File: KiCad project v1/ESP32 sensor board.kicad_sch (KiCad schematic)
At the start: 29 parts, among them J1 USB_C_Receptacle, J3 JST_2mm_LiPo, U1 MCP73871, U2 AMS1117-3.3

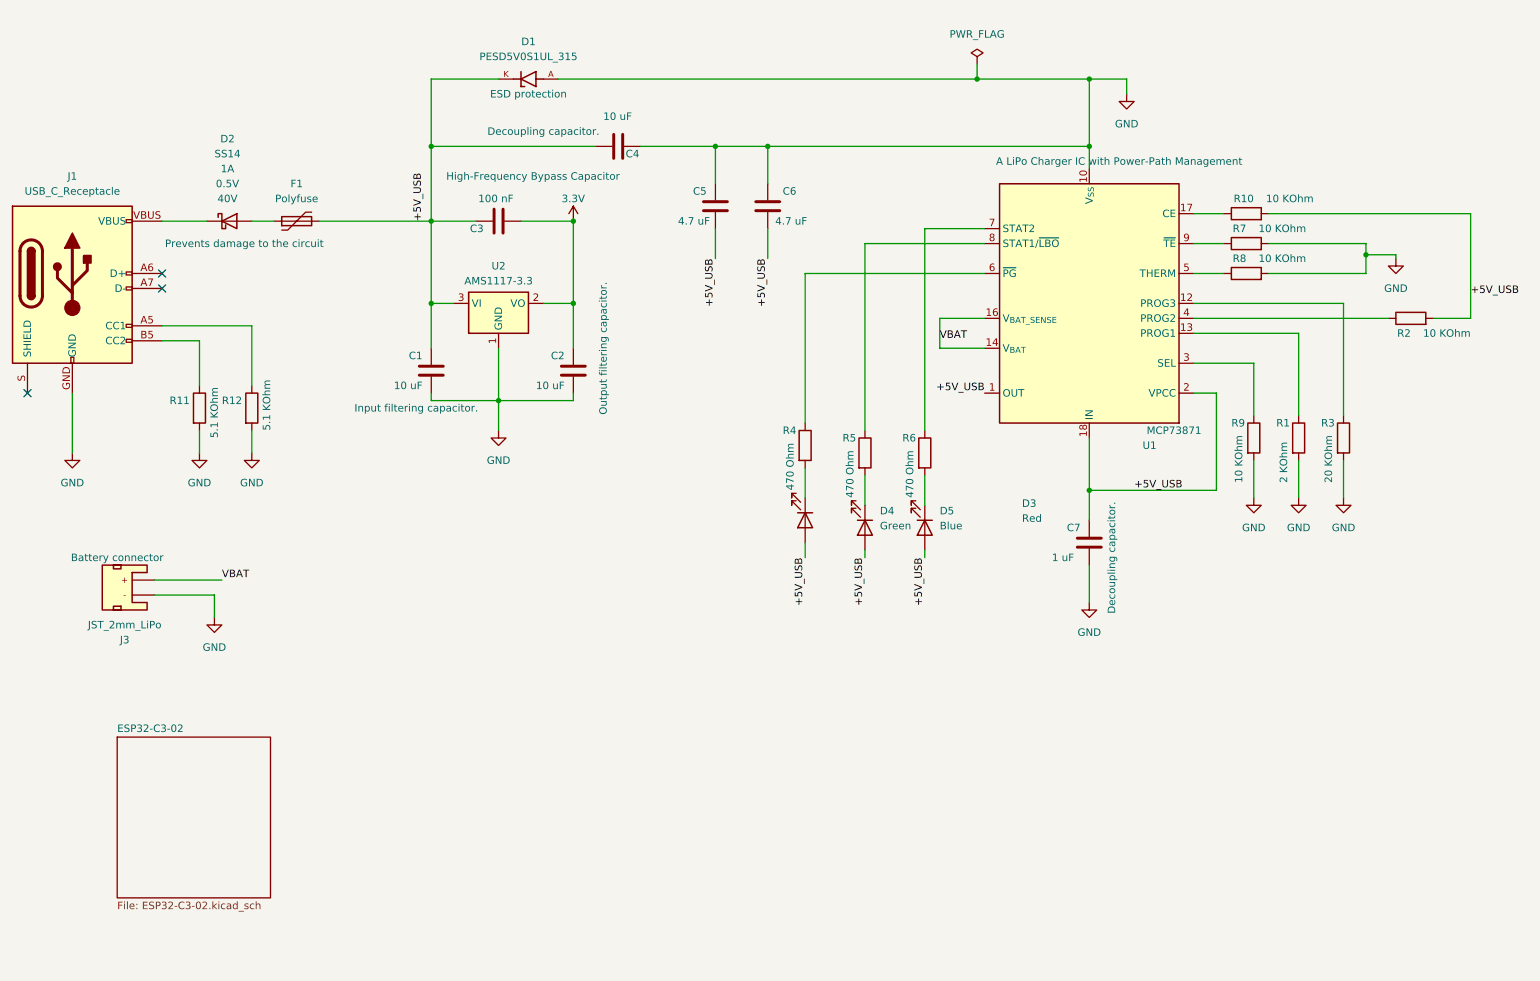
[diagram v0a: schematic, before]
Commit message: Completed first revision of the ESP32 and CP2102 integration.
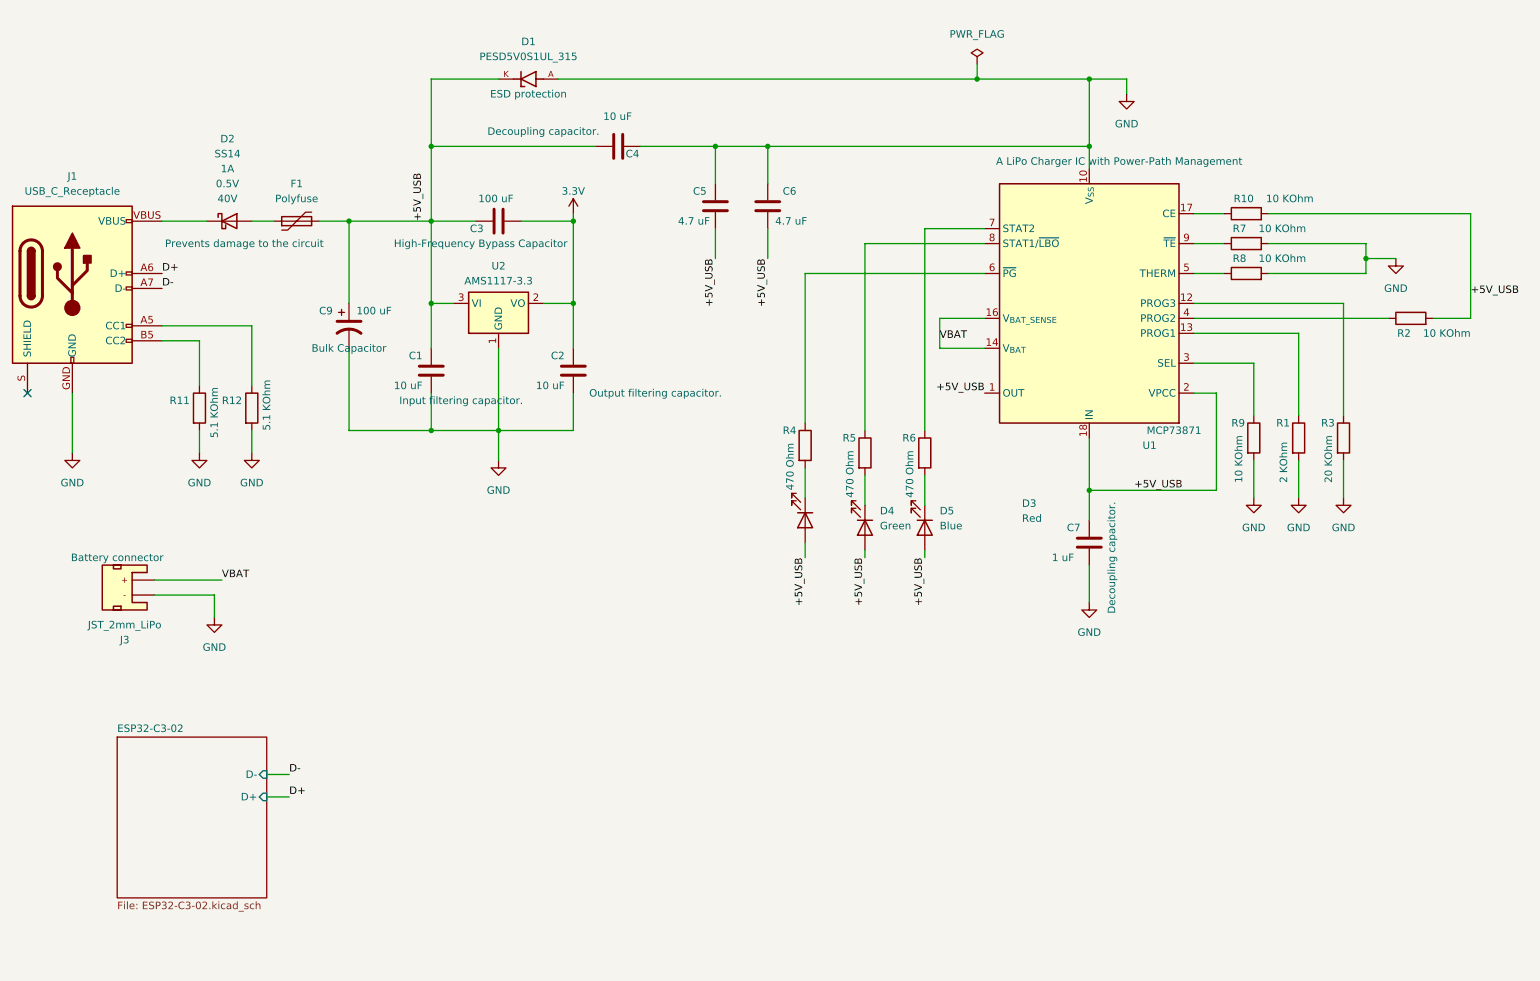
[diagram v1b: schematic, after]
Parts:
- added C9: 100 uF, Capacitor_SMD:C_0805_2012Metric, symbol SparkFun-Capacitor:C_Polarized
- C3: value 100 nF -> 100 uF
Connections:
- net +5V_USB: now also C9.1
- net GND: now also C9.2
- net D+: now reaches J1.A6 (D+), J1.B6 (D+)
- net D-: now reaches J1.A7 (D-), J1.B7 (D-)
- no-connect marks 3 -> 1
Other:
- sheet ESP32-C3-02 ports: added D+, D-; removed none

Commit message: Created the draft layout, and inserted available footprints.
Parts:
- D1: footprint PESD5V0S1UL_315:DIO_PESD5V0S1UL_315 -> Footprints:DIO_PESD5V0S1UL_315
- F1: footprint (none) -> SparkFun-Fuse:1210; symbol Device:Polyfuse -> SparkFun-Fuse:Fuse 6V/2.0A/4.0A; PROD_ID (none) -> RES-14313
- R1, R10, R11, R12, R2, R3, R4, R5, R6, R7, R8, R9: footprint (none) -> Resistor_SMD:R_0805_2012Metric
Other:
- moved on the sheet: F1
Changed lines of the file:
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@@
 			)
 		)
-		(property "Footprint" ""
+		(property "Footprint" "Resistor_SMD:R_0805_2012Metric"
 			(at 236.982 99.06 90)
 			(effects
@@
 			)
 		)
-		(property "Footprint" ""
+		(property "Footprint" "Resistor_SMD:R_0805_2012Metric"
 			(at 229.362 99.06 90)
 			(effects
@@
 			)
 		)
-		(property "Footprint" ""
+		(property "Footprint" "Resistor_SMD:R_0805_2012Metric"
 			(at 229.87 72.898 90)
 			(effects
@@
 			)
 		)
-		(property "Footprint" ""
+		(property "Footprint" "Resistor_SMD:R_0805_2012Metric"
 			(at 153.162 100.33 90)
 			(effects
@@
 			)
 		)
-		(property "Footprint" "PESD5V0S1UL_315:DIO_PESD5V0S1UL_315"
+		(property "Footprint" "Footprints:DIO_PESD5V0S1UL_315"
 			(at 107.95 38.1 0)
 			(effects
@@
 			)
 		)
-		(property "Footprint" ""
+		(property "Footprint" "Resistor_SMD:R_0805_2012Metric"
 			(at 257.81 80.518 90)
 			(effects
@@
 			)
 		)
-		(property "Footprint" ""
+		(property "Footprint" "Resistor_SMD:R_0805_2012Metric"
 			(at 50.292 93.98 90)
 			(effects
@@
 			)
 		)
-		(property "Footprint" ""
+		(property "Footprint" "Resistor_SMD:R_0805_2012Metric"
 			(at 229.87 62.738 90)
 			(effects
@@
 			)
 		)
-		(property "Footprint" ""
+		(property "Footprint" "Resistor_SMD:R_0805_2012Metric"
 			(at 163.322 101.6 90)
 			(effects
@@
 			)
 		)
-		(property "Footprint" ""
+		(property "Footprint" "Resistor_SMD:R_0805_2012Metric"
 			(at 244.602 99.06 90)
 			(effects
@@
 			)
 		)
-		(property "Footprint" ""
+		(property "Footprint" "Resistor_SMD:R_0805_2012Metric"
 			(at 59.182 93.98 90)
 			(effects
@@
 			)
 		)
-		(property "Footprint" ""
+		(property "Footprint" "Resistor_SMD:R_0805_2012Metric"
 			(at 229.87 67.818 90)
 			(effects
@@
 	)
 	(symbol
-		(lib_id "Device:Polyfuse")
-		(at 68.58 62.23 90)
+		(lib_id "SparkFun-Fuse:Fuse 6V/2.0A/4.0A")
+		(at 68.58 62.23 180)
 		(unit 1)
 		(exclude_from_sim no)
@@
 		(fields_autoplaced yes)
 		(property "Reference" "F1"
-			(at 68.58 55.88 90)
+			(at 68.58 55.88 0)
 			(effects
 				(font
@@
 		)
 		(property "Value" "Polyfuse"
-			(at 68.58 58.42 90)
+			(at 68.58 58.42 0)
 			(effects
 				(font
@@
 			)
 		)
-		(property "Footprint" ""
-			(at 73.66 60.96 0)
+		(property "Footprint" "SparkFun-Fuse:1210"
+			(at 68.58 54.61 0)
 			(effects
 				(font
 					(size 1.27 1.27)
 				)
-				(justify left)
 				(hide yes)
 			)
 		)
-		(property "Datasheet" "~"
+		(property "Datasheet" "https://www.belfuse.com/resources/datasheets/circuitprotection/ds-cp-0zch-series.pdf"
+			(at 67.564 56.642 0)
+			(effects
+				(font
+					(size 1.27 1.27)
+				)
+				(hide yes)
+			)
+		)
+		(property "Description" "Resettable fuse 2A"
 			(at 68.58 62.23 0)
 			(effects
@@
 			)
 		)
-		(property "Description" "Resettable fuse, polymeric positive temperature coefficient"
+		(property "Purpose" ""
+			(at 68.58 62.23 0)
+			(effects
+				(font
+					(size 1.27 1.27)
+				)
+			)
+		)
+		(property "Instructions and notes" ""
 			(at 68.58 62.23 0)
 			(effects
@@
 			)
 		)
+		(property "PROD_ID" "RES-14313"
+			(at 68.58 52.07 0)
+			(effects
+				(font
+					(size 1.27 1.27)
+				)
+				(hide yes)
+			)
+		)
 		(pin "1"
 		)
@@
 			)
 		)
-		(property "Footprint" ""
+		(property "Footprint" "Resistor_SMD:R_0805_2012Metric"
 			(at 173.482 101.6 90)
 			(effects

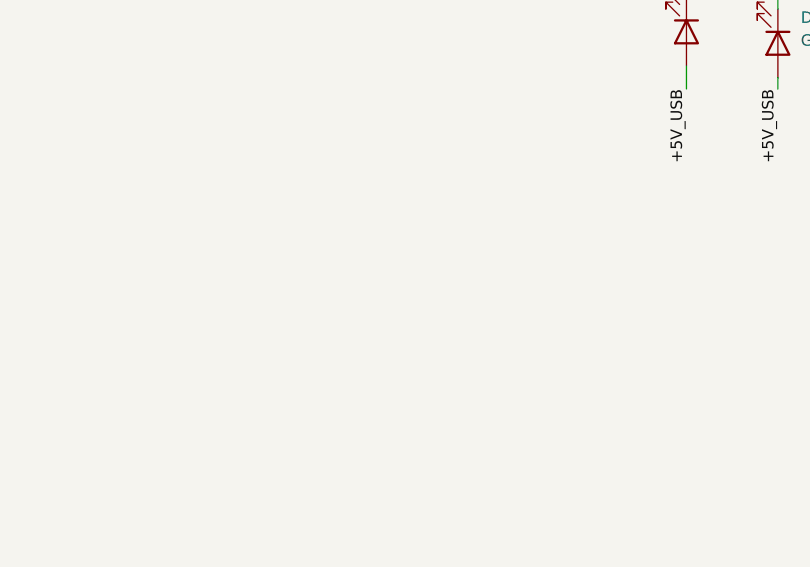
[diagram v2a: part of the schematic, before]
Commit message: Added flash memory module and microsd module to the designed. Moved the libraries and datasheets in the project folder.
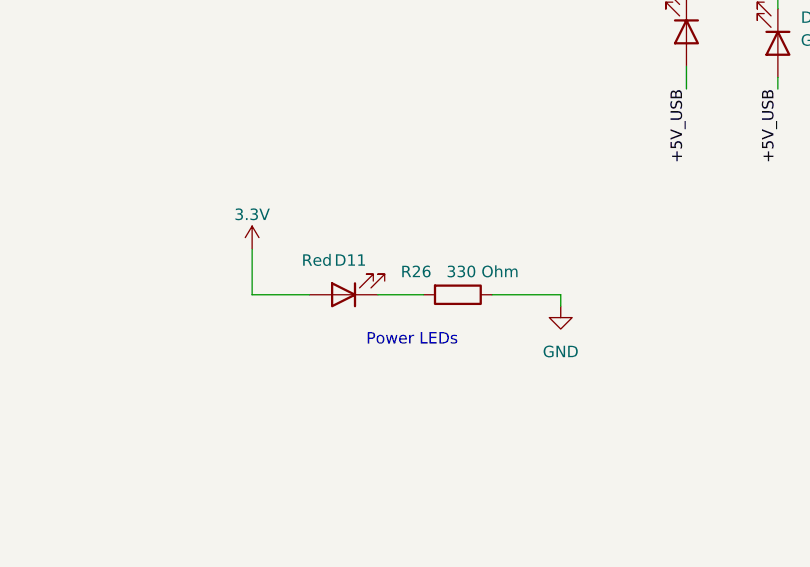
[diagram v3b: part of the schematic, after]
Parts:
- added D11: Red, SparkFun-LED:LED_0603_1608Metric, symbol SparkFun-LED:LED_Red_0603
- added R26: 330 Ohm, Resistor_SMD:R_0805_2012Metric, symbol Device:R
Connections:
- net 3.3V: now also D11.2 (A)
- net GND: now also R26.1
- new net: D11.1 (K), R26.2
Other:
- note added: "Power LEDs"

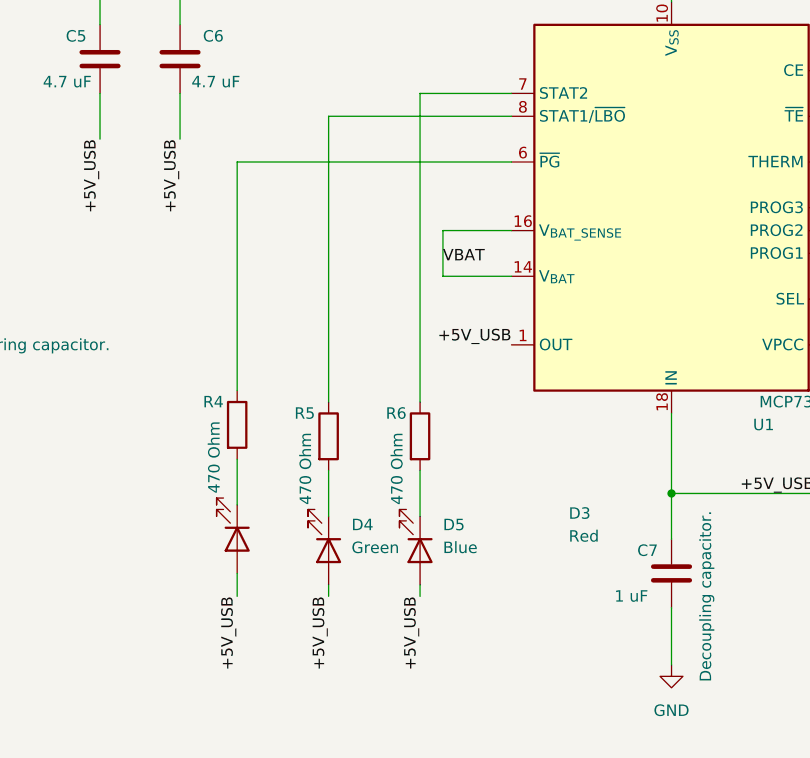
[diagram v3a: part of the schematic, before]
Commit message: Added an OLED I2C display connector, boot and reset buttons, and breakout for remaining pins.
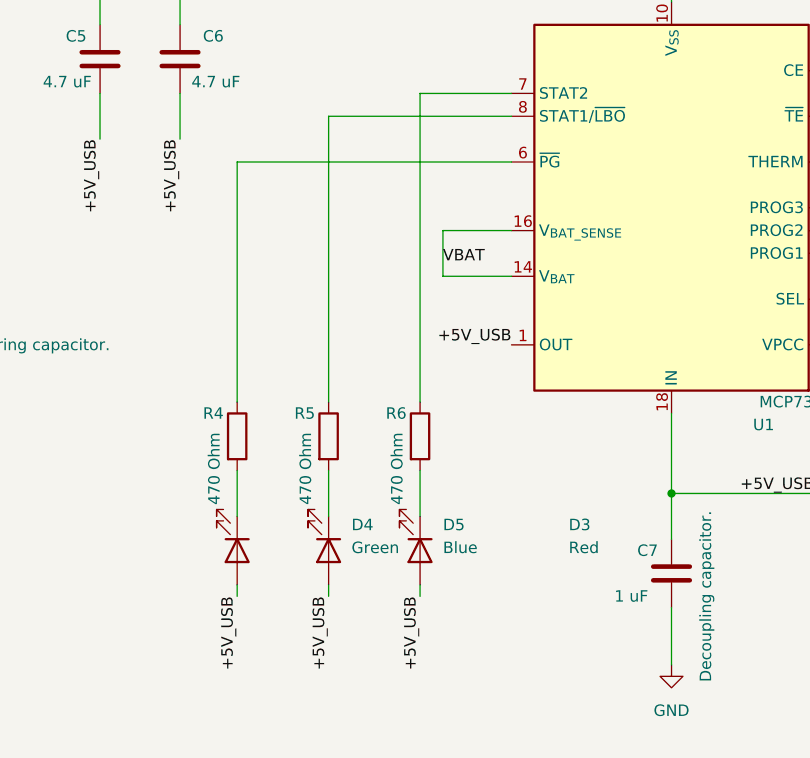
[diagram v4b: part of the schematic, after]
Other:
- moved on the sheet: D3, R4
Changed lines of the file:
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@@
 	(wire
 		(pts
-			(xy 154.94 116.84) (xy 154.94 119.38)
+			(xy 154.94 118.11) (xy 154.94 119.38)
 		)
 		(stroke
@@
 	(wire
 		(pts
-			(xy 154.94 104.14) (xy 154.94 109.22)
+			(xy 154.94 105.41) (xy 154.94 110.49)
 		)
 		(stroke
@@
 	(wire
 		(pts
-			(xy 154.94 96.52) (xy 154.94 71.12)
+			(xy 154.94 97.79) (xy 154.94 71.12)
 		)
 		(stroke
@@
 	(symbol
 		(lib_id "Device:R")
-		(at 154.94 100.33 0)
+		(at 154.94 101.6 0)
 		(unit 1)
 		(exclude_from_sim no)
@@
 		(dnp no)
 		(property "Reference" "R4"
-			(at 151.13 97.79 0)
+			(at 151.13 99.06 0)
 			(effects
 				(font
@@
 		)
 		(property "Value" "470 Ohm"
-			(at 152.4 107.95 90)
+			(at 152.4 109.22 90)
 			(effects
 				(font
@@
 		)
 		(property "Footprint" "Resistor_SMD:R_0805_2012Metric"
-			(at 153.162 100.33 90)
+			(at 153.162 101.6 90)
 			(effects
 				(font
@@
 		)
 		(property "Datasheet" "~"
-			(at 154.94 100.33 0)
+			(at 154.94 101.6 0)
 			(effects
 				(font
@@
 		)
 		(property "Description" "Resistor"
-			(at 154.94 100.33 0)
+			(at 154.94 101.6 0)
 			(effects
 				(font
@@
 		)
 		(property "Purpose" "Current limiting"
-			(at 147.32 105.41 0)
+			(at 147.32 106.68 0)
 			(effects
 				(font
@@
 		)
 		(property "Instructions and notes" ""
-			(at 154.94 100.33 0)
+			(at 154.94 101.6 0)
 			(effects
 				(font
@@
 	(symbol
 		(lib_id "SparkFun-LED:LED_Red_0603")
-		(at 154.94 113.03 270)
+		(at 154.94 114.3 270)
 		(unit 1)
 		(exclude_from_sim no)
@@
 		(dnp no)
 		(property "Reference" "D3"
-			(at 191.77 110.1724 90)
+			(at 191.77 111.4424 90)
 			(effects
 				(font
@@
 		)
 		(property "Value" "Red"
-			(at 191.77 112.7124 90)
+			(at 191.77 113.9824 90)
 			(effects
 				(font
@@
 		)
 		(property "Footprint" "SparkFun-LED:LED_0603_1608Metric"
-			(at 148.59 113.03 0)
+			(at 148.59 114.3 0)
 			(effects
 				(font
@@
 		)
 		(property "Datasheet" "https://docs.broadcom.com/docs/AV02-0551EN"
-			(at 146.05 111.76 0)
+			(at 146.05 113.03 0)
 			(effects
 				(font
@@
 		)
 		(property "Description" "Light emitting diode"
-			(at 154.94 113.03 0)
+			(at 154.94 114.3 0)
 			(effects
 				(font
@@
 		)
 		(property "PROD_ID" "DIO-17976"
-			(at 150.368 113.03 0)
-			(effects
-				(font
+			(at 150.368 114.3 0)
+			(effects
+				(font

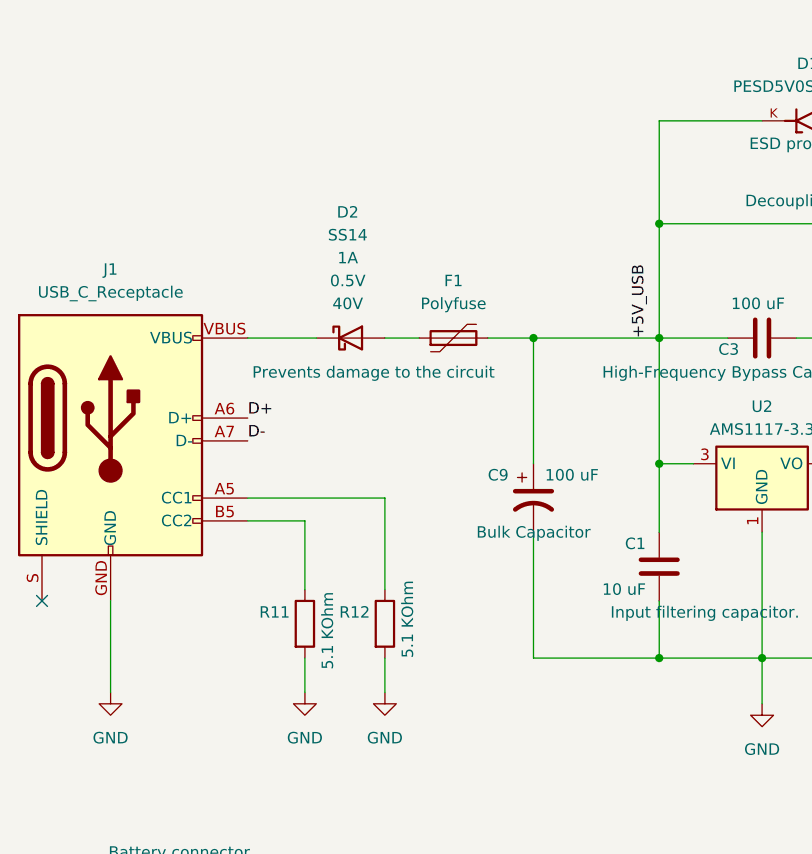
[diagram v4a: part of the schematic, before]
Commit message: Created netclasses and assigned nets.
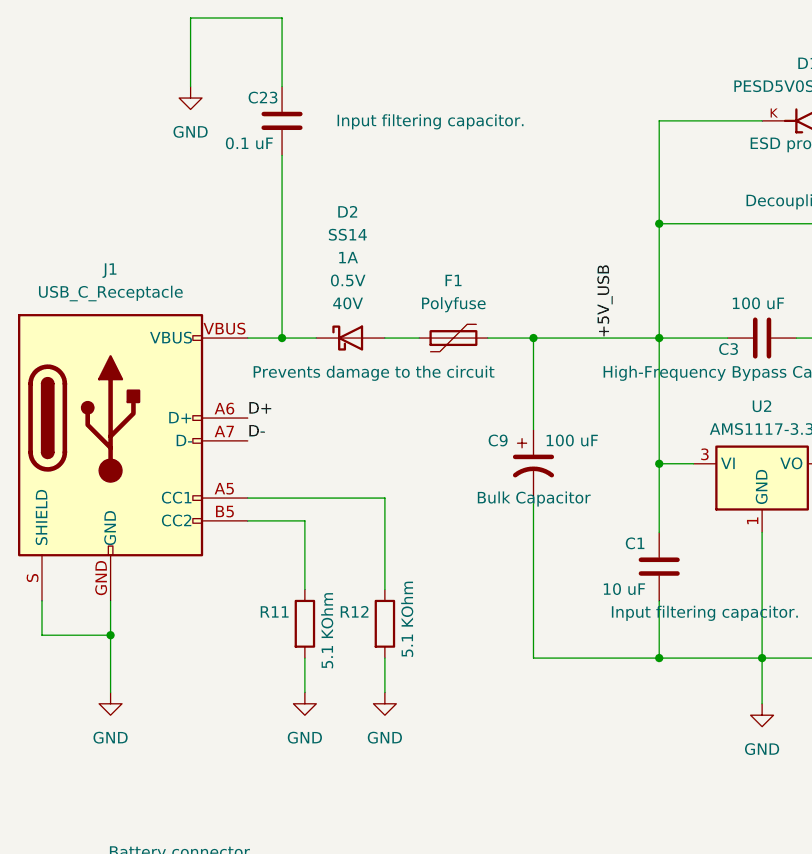
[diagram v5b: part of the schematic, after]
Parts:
- added C23: 0.1 uF, Capacitor_SMD:C_0805_2012Metric, symbol SparkFun-Capacitor:C
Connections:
- net GND: now also J1.S (SHIELD), C23.1
- net at D2.C, J1.VBUS: now also C23.2
- no-connect marks 1 -> 0
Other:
- moved on the sheet: C9
